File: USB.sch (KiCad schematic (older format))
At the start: 44 parts

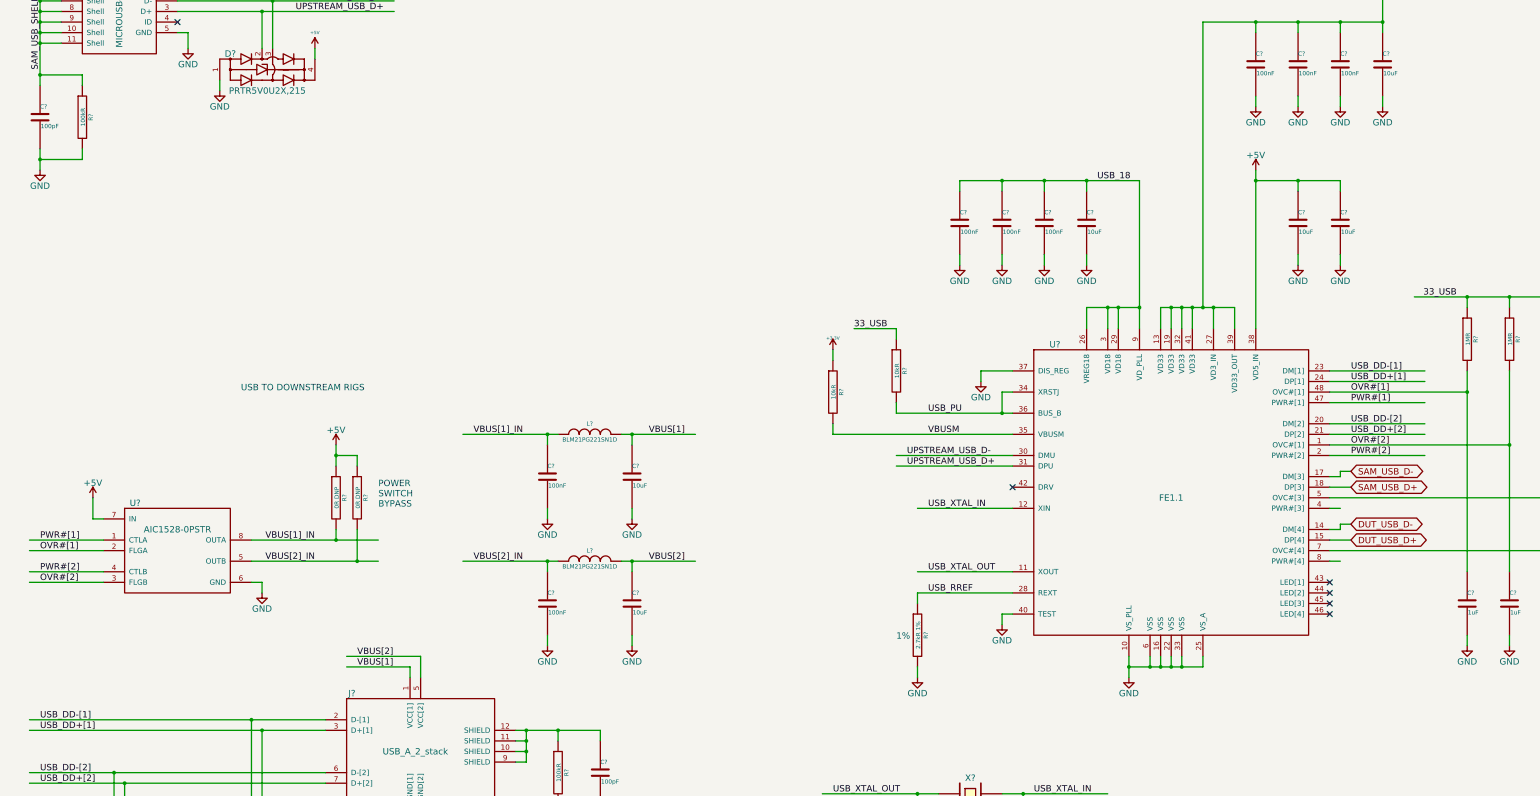
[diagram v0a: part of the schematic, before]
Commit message: connected analog things, lots of testpoints
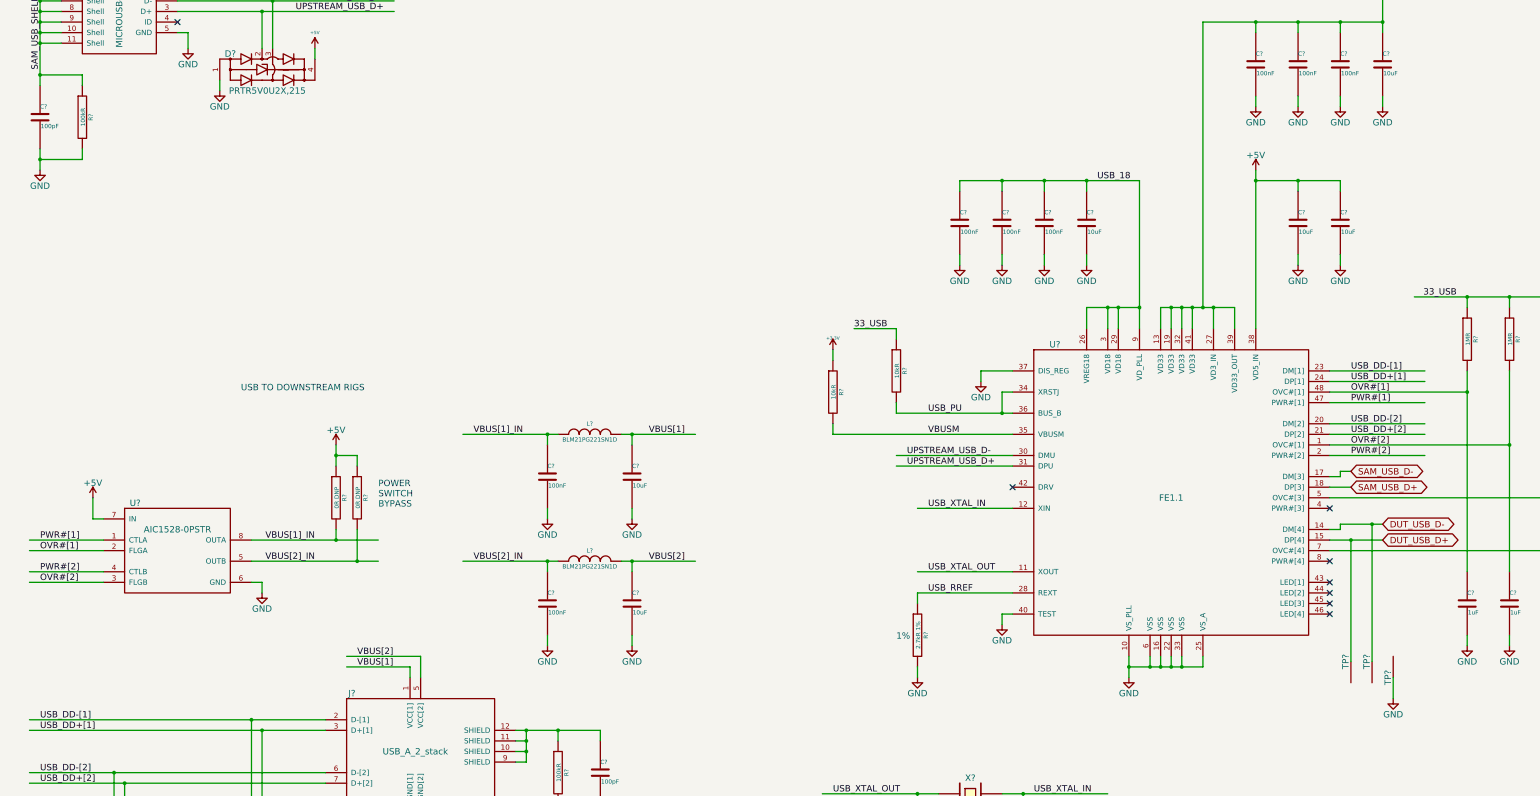
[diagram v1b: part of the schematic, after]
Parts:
- added TP? (x3): TP, symbol TP
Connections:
- wire segments 243 -> 246
- no-connect marks 6 -> 8
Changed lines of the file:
@@
 $Descr B 17000 11000
 encoding utf-8
-Sheet 2 4
+Sheet 2 5
 Title "Tessel 2"
 Date "Thu 12 Mar 2015"
@@
 	13600 6400 15700 6400
 Wire Wire Line
-	13600 6500 13700 6500
-Wire Wire Line
 	13600 6700 13700 6700
 Wire Wire Line
 	13600 6800 13800 6800
 Wire Wire Line
-	13600 7000 13700 7000
+	13800 6800 14100 6800
 Wire Wire Line
 	13300 3500 13300 3400
@@
 	1800 2500 1800 2400
 Wire Wire Line
-	1400 2400 1800 2400
+	1800 2400 1400 2400
 Wire Wire Line
 	1400 1600 1400 1700
@@
 Wire Wire Line
 	13700 6150 13700 6200
-Text GLabel 13800 6800 2    60   BiDi ~ 0
+Text GLabel 14100 6800 2    60   BiDi ~ 0
 DUT_USB_D+
-Text GLabel 13800 6650 2    60   BiDi ~ 0
+Text GLabel 14100 6650 2    60   BiDi ~ 0
 DUT_USB_D-
 Wire Wire Line
-	13800 6650 13700 6650
+	14100 6650 14000 6650
+Wire Wire Line
+	14000 6650 13700 6650
 Wire Wire Line
 	13700 6650 13700 6700
@@
 Text Label 2800 1600 0    60   ~ 0
 V_USB_IN
+$Comp
+L TP TP?
+U 1 1 55416368
+P 13800 7950
+F 0 "TP?" H 13800 8000 60  0000 C CNN
+F 1 "TP" H 13800 7900 60  0001 C CNN
+F 2 "" H 13800 7950 60  0000 C CNN
+F 3 "" H 13800 7950 60  0000 C CNN
+	1    13800 7950
+	0    -1   1    0
+$EndComp
+$Comp
+L TP TP?
+U 1 1 5541650C
+P 14000 7950
+F 0 "TP?" H 14000 8000 60  0000 C CNN
+F 1 "TP" H 14000 7900 60  0001 C CNN
+F 2 "" H 14000 7950 60  0000 C CNN
+F 3 "" H 14000 7950 60  0000 C CNN
+	1    14000 7950
+	0    -1   1    0
+$EndComp
+Wire Wire Line
+	14000 7950 14000 6650
+Connection ~ 14000 6650
+Wire Wire Line
+	13800 7950 13800 6800
+Connection ~ 13800 6800
+$Comp
+L TP TP?
+U 1 1 55416AD9
+P 14200 8100
+F 0 "TP?" H 14200 8150 60  0000 C CNN
+F 1 "TP" H 14200 8050 60  0001 C CNN
+F 2 "" H 14200 8100 60  0000 C CNN
+F 3 "" H 14200 8100 60  0000 C CNN
+	1    14200 8100
+	0    -1   -1   0
+$EndComp
+$Comp
+L GND #PWR?
+U 1 1 55416BCA
+P 14200 8300
+F 0 "#PWR?" H 14200 8050 60  0001 C CNN
+F 1 "GND" H 14200 8150 60  0000 C CNN
+F 2 "" H 14200 8300 60  0000 C CNN
+F 3 "" H 14200 8300 60  0000 C CNN
+	1    14200 8300
+	1    0    0    -1
+$EndComp
+Wire Wire Line
+	14200 8300 14200 8100
+NoConn ~ 13600 7000
+NoConn ~ 13600 6500
 $EndSCHEMATC

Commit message: moved a bunch of things around inside the schematics
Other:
- moved on the sheet: C?
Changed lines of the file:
@@
 Text Label 13800 5900 0    60   ~ 0
 OVR#[2]
-Text Label 11400 3400 0    60   ~ 0
+Text Label 11800 3400 2    60   ~ 0
 USB_18
 $Comp
@@
 L TM_C C?
 U 1 1 54EDB9F5
-P 11300 3800
-F 0 "C?" H 11300 3900 40  0000 L CNN
-F 1 "10uF" H 11306 3715 40  0000 L CNN
-F 2 "tm-kicad-lib:SMD-0805-C" H 11338 3650 30  0001 C CNN
-F 3 "" H 11300 3800 60  0000 C CNN
-	1    11300 3800
+P 11400 3800
+F 0 "C?" H 11400 3900 40  0000 L CNN
+F 1 "10uF" H 11406 3715 40  0000 L CNN
+F 2 "tm-kicad-lib:SMD-0805-C" H 11438 3650 30  0001 C CNN
+F 3 "" H 11400 3800 60  0000 C CNN
+	1    11400 3800
 	1    0    0    -1
 $EndComp
@@
 L TM_C C?
 U 1 1 54EDB9FC
-P 10900 3800
-F 0 "C?" H 10900 3900 40  0000 L CNN
-F 1 "100nF" H 10906 3715 40  0000 L CNN
-F 2 "tm-kicad-lib:SMD-0402-C" H 10938 3650 30  0001 C CNN
-F 3 "" H 10900 3800 60  0000 C CNN
-	1    10900 3800
+P 11000 3800
+F 0 "C?" H 11000 3900 40  0000 L CNN
+F 1 "100nF" H 11006 3715 40  0000 L CNN
+F 2 "tm-kicad-lib:SMD-0402-C" H 11038 3650 30  0001 C CNN
+F 3 "" H 11000 3800 60  0000 C CNN
+	1    11000 3800
 	1    0    0    -1
 $EndComp
@@
 L TM_C C?
 U 1 1 54EDBA03
-P 10500 3800
-F 0 "C?" H 10500 3900 40  0000 L CNN
-F 1 "100nF" H 10506 3715 40  0000 L CNN
-F 2 "tm-kicad-lib:SMD-0402-C" H 10538 3650 30  0001 C CNN
-F 3 "" H 10500 3800 60  0000 C CNN
-	1    10500 3800
+P 10600 3800
+F 0 "C?" H 10600 3900 40  0000 L CNN
+F 1 "100nF" H 10606 3715 40  0000 L CNN
+F 2 "tm-kicad-lib:SMD-0402-C" H 10638 3650 30  0001 C CNN
+F 3 "" H 10600 3800 60  0000 C CNN
+	1    10600 3800
 	1    0    0    -1
 $EndComp
@@
 L TM_C C?
 U 1 1 54EDBA0A
-P 10100 3800
-F 0 "C?" H 10100 3900 40  0000 L CNN
-F 1 "100nF" H 10106 3715 40  0000 L CNN
-F 2 "tm-kicad-lib:SMD-0402-C" H 10138 3650 30  0001 C CNN
-F 3 "" H 10100 3800 60  0000 C CNN
-	1    10100 3800
+P 10200 3800
+F 0 "C?" H 10200 3900 40  0000 L CNN
+F 1 "100nF" H 10206 3715 40  0000 L CNN
+F 2 "tm-kicad-lib:SMD-0402-C" H 10238 3650 30  0001 C CNN
+F 3 "" H 10200 3800 60  0000 C CNN
+	1    10200 3800
 	1    0    0    -1
 $EndComp
@@
 L GND #PWR?
 U 1 1 54EB6EE4
-P 10100 4200
-F 0 "#PWR?" H 10100 3950 60  0001 C CNN
-F 1 "GND" H 10100 4050 60  0000 C CNN
-F 2 "" H 10100 4200 60  0000 C CNN
-F 3 "" H 10100 4200 60  0000 C CNN
-	1    10100 4200
+P 10200 4200
+F 0 "#PWR?" H 10200 3950 60  0001 C CNN
+F 1 "GND" H 10200 4050 60  0000 C CNN
+F 2 "" H 10200 4200 60  0000 C CNN
+F 3 "" H 10200 4200 60  0000 C CNN
+	1    10200 4200
 	1    0    0    -1
 $EndComp
@@
 L GND #PWR?
 U 1 1 54EB6F1C
-P 10500 4200
-F 0 "#PWR?" H 10500 3950 60  0001 C CNN
-F 1 "GND" H 10500 4050 60  0000 C CNN
-F 2 "" H 10500 4200 60  0000 C CNN
-F 3 "" H 10500 4200 60  0000 C CNN
-	1    10500 4200
+P 10600 4200
+F 0 "#PWR?" H 10600 3950 60  0001 C CNN
+F 1 "GND" H 10600 4050 60  0000 C CNN
+F 2 "" H 10600 4200 60  0000 C CNN
+F 3 "" H 10600 4200 60  0000 C CNN
+	1    10600 4200
 	1    0    0    -1
 $EndComp
@@
 L GND #PWR?
 U 1 1 54EB6F22
-P 10900 4200
-F 0 "#PWR?" H 10900 3950 60  0001 C CNN
-F 1 "GND" H 10900 4050 60  0000 C CNN
-F 2 "" H 10900 4200 60  0000 C CNN
-F 3 "" H 10900 4200 60  0000 C CNN
-	1    10900 4200
+P 11000 4200
+F 0 "#PWR?" H 11000 3950 60  0001 C CNN
+F 1 "GND" H 11000 4050 60  0000 C CNN
+F 2 "" H 11000 4200 60  0000 C CNN
+F 3 "" H 11000 4200 60  0000 C CNN
+	1    11000 4200
 	1    0    0    -1
 $EndComp
@@
 L GND #PWR?
 U 1 1 54EB6F5A
-P 11300 4200
-F 0 "#PWR?" H 11300 3950 60  0001 C CNN
-F 1 "GND" H 11300 4050 60  0000 C CNN
-F 2 "" H 11300 4200 60  0000 C CNN
-F 3 "" H 11300 4200 60  0000 C CNN
-	1    11300 4200
+P 11400 4200
+F 0 "#PWR?" H 11400 3950 60  0001 C CNN
+F 1 "GND" H 11400 4050 60  0000 C CNN
+F 2 "" H 11400 4200 60  0000 C CNN
+F 3 "" H 11400 4200 60  0000 C CNN
+	1    11400 4200
 	1    0    0    -1
 $EndComp
@@
 Connection ~ 12900 3400
 Wire Wire Line
-	10100 4200 10100 4100
-Wire Wire Line
-	10900 4200 10900 4100
-Wire Wire Line
-	10500 4200 10500 4100
-Wire Wire Line
-	11300 4200 11300 4100
-Wire Wire Line
-	10100 3400 10500 3400
-Wire Wire Line
-	10500 3400 10900 3400
-Wire Wire Line
-	10900 3400 11300 3400
-Wire Wire Line
-	11300 3400 11800 3400
-Wire Wire Line
-	11300 3400 11300 3500
-Wire Wire Line
-	10900 3500 10900 3400
-Connection ~ 10900 3400
-Wire Wire Line
-	10500 3500 10500 3400
-Connection ~ 10500 3400
-Wire Wire Line
-	10100 3500 10100 3400
-Connection ~ 11300 3400
+	10200 4200 10200 4100
+Wire Wire Line
+	11000 4200 11000 4100
+Wire Wire Line
+	10600 4200 10600 4100
+Wire Wire Line
+	11400 4200 11400 4100
+Wire Wire Line
+	10200 3400 10600 3400
+Wire Wire Line
+	10600 3400 11000 3400
+Wire Wire Line
+	11000 3400 11400 3400
+Wire Wire Line
+	11400 3400 11800 3400
+Wire Wire Line
+	11400 3400 11400 3500
+Wire Wire Line
+	11000 3500 11000 3400
+Connection ~ 11000 3400
+Wire Wire Line
+	10600 3500 10600 3400
+Connection ~ 10600 3400
+Wire Wire Line
+	10200 3500 10200 3400
+Connection ~ 11400 3400
 Wire Wire Line
 	13300 2700 13300 2600

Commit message: schematic check with kevin. misc fixes, mostly on usb
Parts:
- removed R?: 0R DNP, tm-kicad-lib:SMD-0603-R, symbol TM_R
- added J?: CONN_01X02, symbol CONN_01X02
- added JP?: JUMPER, symbol JUMPER
- added R?: 100kR, tm-kicad-lib:SMD-0402-R, symbol TM_R
- C?: value 1uF -> 1uF DNP
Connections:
- net labels removed: +3.3V
- wire segments 246 -> 250
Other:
- moved on the sheet: C?, D?, J?, R?

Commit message: passed schematic review
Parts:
- removed TP? (x3): TP, symbol TP
- added C?: 100pF, tm-kicad-lib:SMD-0402-C, symbol TM_C
- added J?: USB_A, symbol USB_A
- added R?: 100kR, tm-kicad-lib:SMD-0402-R, symbol TM_R
- C?: value 1uF -> 1uF DNP
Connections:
- net labels added: UUT_USB_D+, UUT_USB_D-, UUT_USB_SHELL, UUT_VINUSB
- net labels removed: DUT_USB_D+, DUT_USB_D-
- wire segments 250 -> 261
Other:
- moved on the sheet: C?, D?, J?, JP?, R?
